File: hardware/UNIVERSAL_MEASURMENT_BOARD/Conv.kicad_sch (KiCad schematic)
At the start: 25 parts, among them U10 LMR50410YFQDBVRQ1, U7 LMR50410Y5FQDBVRQ1, U8 RAA2114034GP3#JA0, U9 LMR50410YFQDBVRQ1

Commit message: continued
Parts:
- removed D1: DS, symbol Device:D_Schottky
- removed L1, L2, L3, L4: L_Small, symbol Device:L_Small
- removed U10, U9: LMR50410YFQDBVRQ1, SOT95P280X145-6N, symbol LMR50410YFQDBVRQ1:LMR50410YFQDBVRQ1
- removed U7: LMR50410Y5FQDBVRQ1, SOT95P280X145-6N, symbol LMR50410Y5FQDBVRQ1:LMR50410Y5FQDBVRQ1
- removed U8: RAA2114034GP3#JA0, SOT95P280X110-5N, symbol RAA2114034GP3#JA0:RAA2114034GP3#JA0
- added C14, C17, C19, C20, C32, C34, C37, C38, C39, C40, C41, C42, C45, C47, C48, C50, C51, C52: 22uF, Capacitor_SMD:C_0805_2012Metric, symbol Device:C_Small
- added C15, C43: 330nF, Capacitor_SMD:C_0805_2012Metric, symbol Device:C_Small
- added C16, C35, C44, C53, C55: 100nF, Capacitor_SMD:C_0805_2012Metric, symbol Device:C_Small
- added C18, C33, C46, C49: 100nF, Capacitor_SMD:C_0603_1608Metric, symbol Device:C_Small
- added C36: 10uF, Capacitor_SMD:C_0805_2012Metric, symbol Device:C_Small
- added C54, C56: 10uF, symbol Device:C_Polarized_Small
- added C57: -F, Capacitor_SMD:C_0805_2012Metric, symbol Device:C_Small
- added F38: -A, symbol Device:Fuse_Small
- added L1, L2, L3: 68uH/1.4A, Inductor_SMD:L_TDK_VLS6045EX_VLS6045AF, symbol Samacsys_kicad_sym:SRR4028-271Y
- added R10, R12, R2, R8: 43kR, symbol Device:R
- added R11, R13, R9: -R, symbol Device:R
- added U10, U12, U7: TPS54202HDDCR, SOT95P280X110-6N, symbol TPS54202HDDCR:TPS54202HDDCR
- added U11: L7915, symbol Regulator_Linear:L7915
- added U13: ICL7662EBA+, SOIC127P600X175-8N, symbol ICL7662EBA+:ICL7662EBA+
- added U6: L7815, symbol Regulator_Linear:L7815
- added U8, U9: AMS1117-3.3, Package_TO_SOT_SMD:SOT-223-3_TabPin2, symbol Regulator_Linear:AMS1117-3.3
- C21: value 4.7uF -> 100nF; footprint (none) -> Capacitor_SMD:C_0603_1608Metric; Manufacturer_Name (none) -> --; Manufacturer_Part_Number (none) -> C0603C104J3RACTU; Mouser Part Number (none) -> --; Mouser Price/Stock (none) -> https://www.mouser.pl/ProductDetail/KEMET/C0603C104J3RACTU?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
- C22, C27, C28: footprint (none) -> Capacitor_SMD:C_0805_2012Metric; Manufacturer_Name (none) -> MCASH21GCC7684MTCA1J; Manufacturer_Part_Number (none) -> CL21A107MQYNNWE; Mouser Part Number (none) -> 810-C2012X5R1V226MAC
- C23, C26, C29: value 2.2uF -> 22uF; footprint (none) -> Capacitor_SMD:C_0805_2012Metric; Manufacturer_Name (none) -> MCASH21GCC7684MTCA1J; Manufacturer_Part_Number (none) -> CL21A107MQYNNWE; Mouser Part Number (none) -> 810-C2012X5R1V226MAC
- C24: value 100nF -> 22uF; footprint (none) -> Capacitor_SMD:C_0805_2012Metric; Manufacturer_Name (none) -> MCASH21GCC7684MTCA1J; Manufacturer_Part_Number (none) -> CL21A107MQYNNWE; Mouser Part Number (none) -> 810-C2012X5R1V226MAC
- C25, C31: value 10uF -> 22uF; footprint (none) -> Capacitor_SMD:C_0805_2012Metric; Manufacturer_Name (none) -> MCASH21GCC7684MTCA1J; Manufacturer_Part_Number (none) -> CL21A107MQYNNWE; Mouser Part Number (none) -> 810-C2012X5R1V226MAC
- C30: footprint (none) -> Capacitor_SMD:C_0603_1608Metric; Manufacturer_Name (none) -> --; Manufacturer_Part_Number (none) -> C0603C104J3RACTU; Mouser Part Number (none) -> --; Mouser Price/Stock (none) -> https://www.mouser.pl/ProductDetail/KEMET/C0603C104J3RACTU?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
- R3: value 1MR -> -R
- R4, R6: value R -> 43kR
- R5, R7: value R -> -R
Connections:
- net +12V: now also C22.1, C23.1, C24.1, C25.1, R3.2, L1.2; no longer C28.1, C31.1, R4.2, R6.2
- net +24V: now also C47.2, C48.2, C49.2, R10.1, U12.3 (VIN); no longer C21.1, C23.1, C26.1, C29.1, R3.2
- net +3.3V: now also C28.1, C29.1, U8.2 (VO); no longer C22.1
- net +5V: now also C26.1, C27.1, R7.2, C34.1, C35.1, C38.1, C39.1, C40.1, C41.1, L2.2, U8.3 (VI), U9.3 (VI); no longer C25.1
- net GND: now also C21.1, C24.2, C27.2, C31.1, R4.1, C14.2, C15.2, C16.2, C17.2, C19.1, C20.1, C32.1, C33.1, C34.2, C35.2, C36.2, C37.2, C38.2, C39.2, C40.2, C41.2, C42.2, C43.2, C44.2, C45.2, C47.1, C48.1, C49.1, C50.2, C51.2, C52.2, C53.2, C55.2, C56.1, C57.2, R12.1, R13.1, R8.1, R9.1, U10.1 (GND), U11.1 (GND), U12.1 (GND), U13.3 (GND), U6.2 (GND), U7.1 (GND), U8.1 (GND), U9.1 (GND); no longer C21.2, C31.2, R7.1
- net at C30.1: now also U10.6 (BOOT)
- net at C30.2: now also L2.1, U10.2 (SW)
- net +18V: now reaches R6.1
- net +18V: now also C21.2, C31.2, C14.1, C15.1, C19.2, C20.2, C32.2, C33.2, C52.1, C53.1, F38.2, R2.1, U10.3 (VIN), U13.8 (V+), U6.1 (IN), U7.3 (VIN); no longer R7.2
- net at R5.2: now also R3.1, U7.4 (FB); no longer R4.1
- new net: R2.2, R4.2, U7.5 (EN)
- new net: C18.1, U7.6 (BOOT)
- new net: C18.2, L1.1, U7.2 (SW)
- new net: C50.1, C51.1, F38.1, L3.2, R11.2
- new net: R10.2, R12.2, U12.5 (EN)
- new net: C54.1, U13.2 (CAP+)
- new net: C54.2, U13.4 (CAP-)
- new net: R6.2, R8.2, U10.5 (EN)
- new net: R11.1, R13.2, U12.4 (FB)
- new net: R7.1, R9.2, U10.4 (FB)
- new net: C57.1, U13.7 (OSC)
- new net: C46.1, U12.6 (BOOT)
- new net: C46.2, L3.1, U12.2 (SW)
- new net +15VA: C16.1, C17.1, U6.3 (OUT)
- new net +3.3VA: C36.1, C37.1, U9.2 (VO)
- new net -15VA: C44.1, C45.1, U11.3 (VO)
- new net -18V: C42.1, C43.1, C55.1, C56.2, U11.2 (VI), U13.5 (VOUT)
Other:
- note added: "+12V"
- note added: "+15V LDO"
- note added: "+15VA"
- note added: "+18V"
- note added: "+3.3V"
- note added: "+3.3VA"
- note added: "+5.0V"
- note added: "-15V LDO"
- note added: "-15VA"
- note added: "-18V"
- note added: "-18V INV"
- note added: "12V"
- note added: "12V DC/DC"
- note added: "18V DC/DC"
- note added: "24VIN"
- note added: "3V3 LDO"
- note added: "3V3A"
- note added: "5V"
- note added: "5V DC/DC"
- note added: "ANALOG"
- note added: "DC/DC Converters"
- note added: "DIGITAL"
- note added: "Linear Converters"
- note added: "Power Section Diagram"
- note removed: "12V0"
- note removed: "5V0"
- company: (none) -> PUT Motorsport Formula Student team
- title: (none) -> Universal Measurment Board

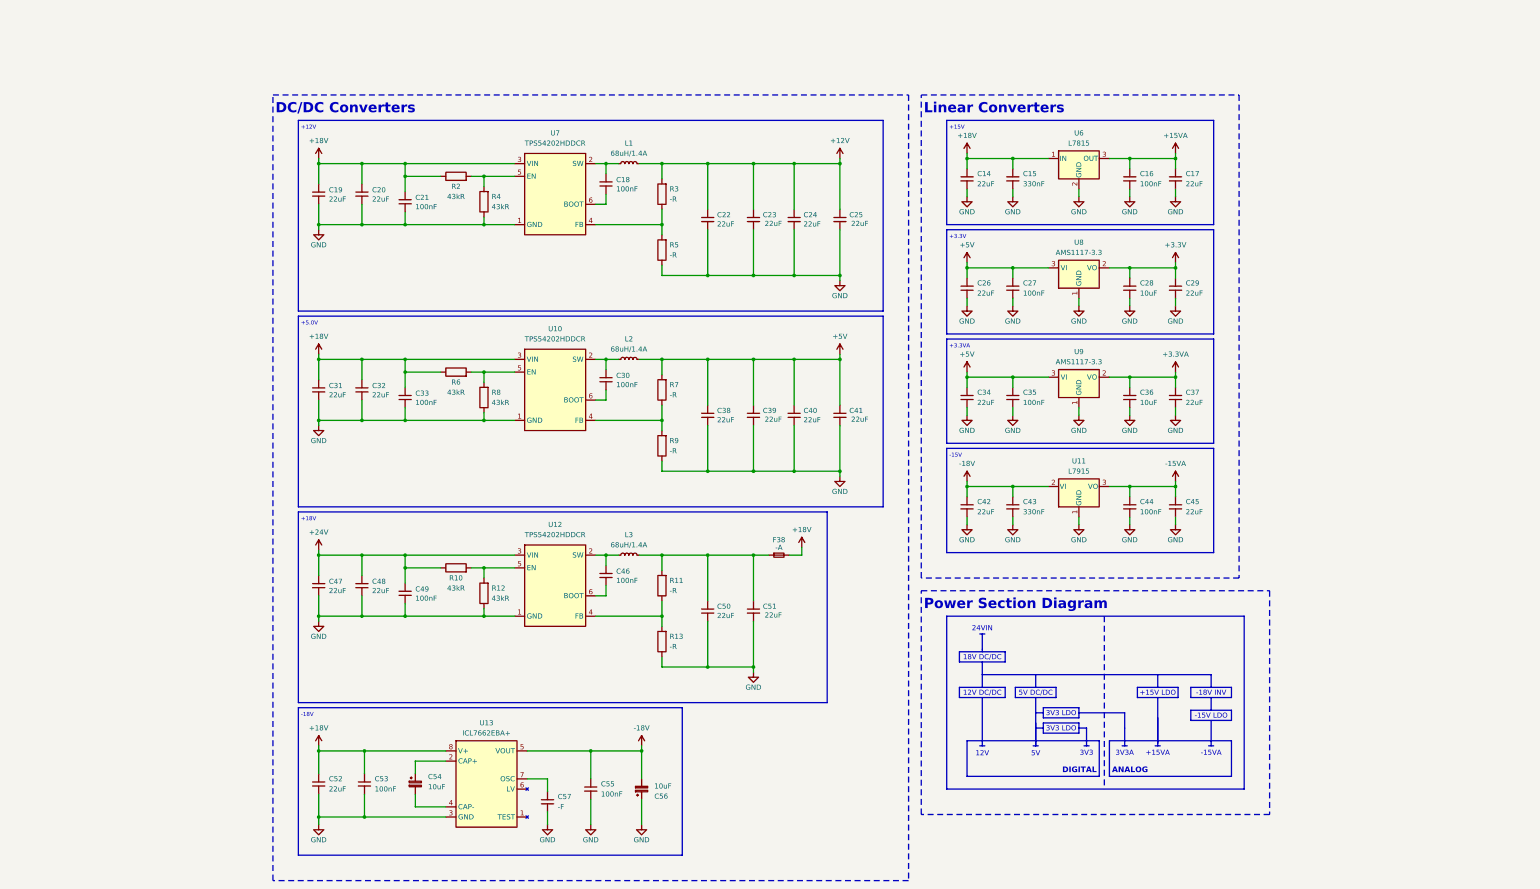
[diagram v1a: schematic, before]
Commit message: schematic review corrections
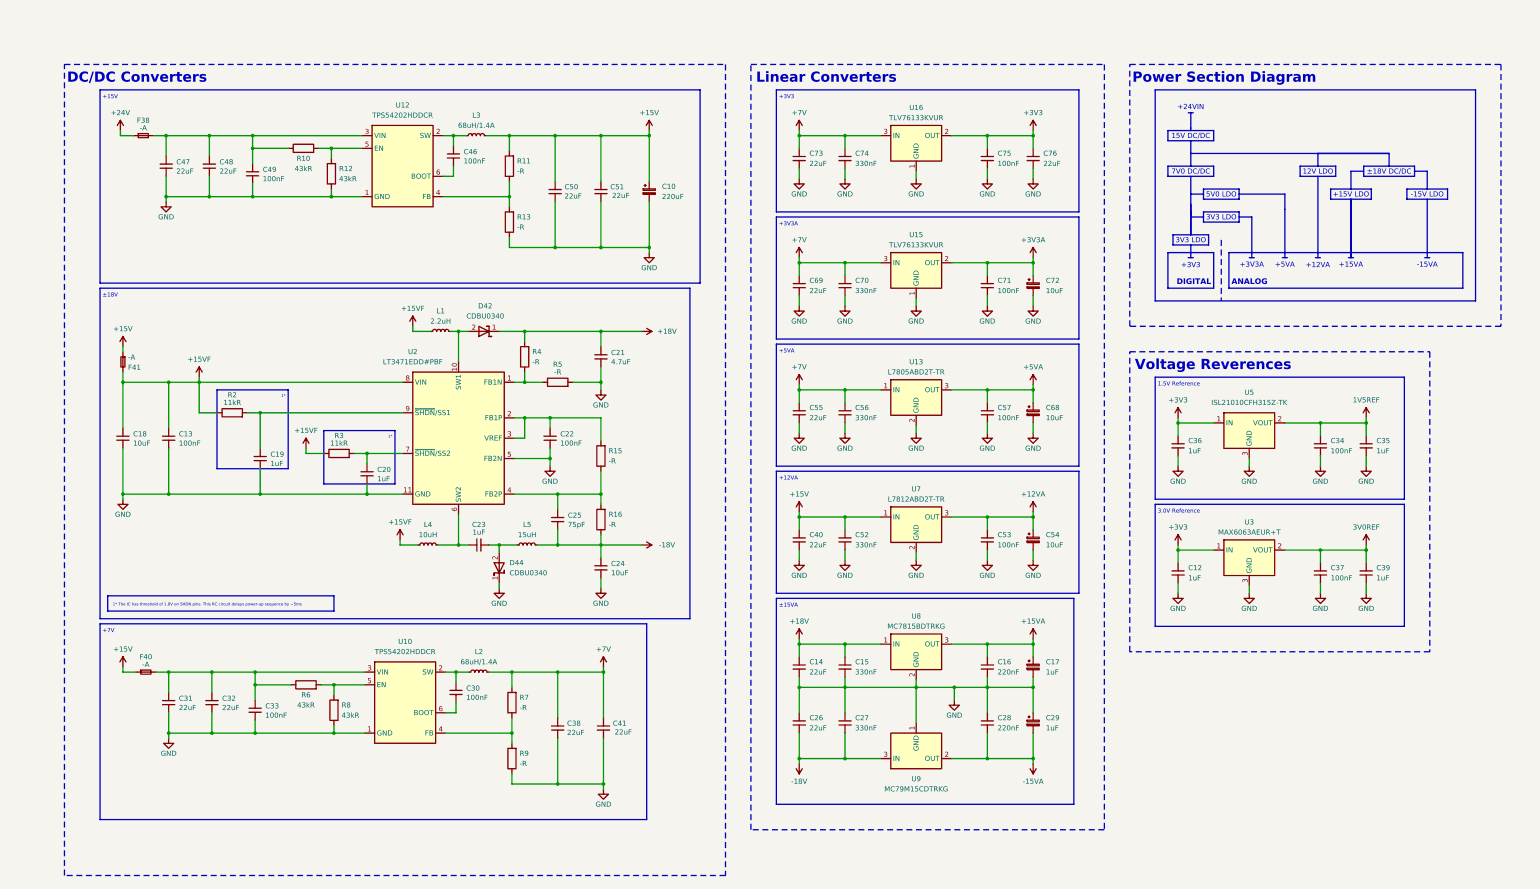
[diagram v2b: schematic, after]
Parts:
- removed C17, C29, C42, C45: 22uF, Capacitor_SMD:C_0805_2012Metric, symbol Device:C_Small
- removed C43: 330nF, Capacitor_SMD:C_0805_2012Metric, symbol Device:C_Small
- removed C44: 100nF, Capacitor_SMD:C_0805_2012Metric, symbol Device:C_Small
- removed C56: 10uF, symbol Device:C_Polarized_Small
- removed U11: L7915, symbol Regulator_Linear:L7915
- removed U13: ICL7662EBA+, SOIC127P600X175-8N, symbol ICL7662EBA+:ICL7662EBA+
- removed U6: L7815, symbol Regulator_Linear:L7815
- removed U7: TPS54202HDDCR, SOT95P280X110-6N, symbol TPS54202HDDCR:TPS54202HDDCR
- removed U8, U9: AMS1117-3.3, Package_TO_SOT_SMD:SOT-223-3_TabPin2, symbol Regulator_Linear:AMS1117-3.3
- added C10: 220uF, symbol Device:C_Polarized_Small
- added C12: 1uF, Capacitor_SMD:C_0805_2012Metric, symbol Device:C_Small
- added C13, C71, C75: 100nF, Capacitor_SMD:C_0805_2012Metric, symbol Device:C_Small
- added C17, C29: 1uF, symbol Device:C_Polarized_Small
- added C56, C70, C74: 330nF, Capacitor_SMD:C_0805_2012Metric, symbol Device:C_Small
- added C68, C72: 10uF, symbol Device:C_Polarized_Small
- added C69, C73, C76: 22uF, Capacitor_SMD:C_0805_2012Metric, symbol Device:C_Small
- added D42, D44: CDBU0340, DIOM179X85N, symbol CDBU0340:CDBU0340
- added F40, F41: -A, symbol Device:Fuse_Small
- added L4: 10uH, Inductor_SMD:L_TDK_VLS6045EX_VLS6045AF, symbol Samacsys_kicad_sym:SRR4028-271Y
- added L5: 15uH, Inductor_SMD:L_TDK_VLS6045EX_VLS6045AF, symbol Samacsys_kicad_sym:SRR4028-271Y
- added R15, R16: -R, symbol Device:R
- added U13: L7805ABD2T-TR, L7805ABD2TTR, symbol L7805ABD2T-TR:L7805ABD2T-TR
- added U15, U16: TLV76133KVUR, TLV76133KVUR, symbol TLV76133KVUR:TLV76133KVUR
- added U2: LT3471EDD#PBF, SON50P300X300X80-11N-D, symbol LT3471EDD#PBF:LT3471EDD#PBF
- added U3: MAX6063AEUR+T, SOT95P229X119-3N, symbol MAX6063AEUR+T:MAX6063AEUR+T
- added U5: ISL21010CFH315Z-TK, SOT95P237X112-3N, symbol ISL21010CFH315Z-TK:ISL21010CFH315Z-TK
- added U7: L7812ABD2T-TR, L7812ABD2TTR, symbol L7812ABD2T-TR:L7812ABD2T-TR
- added U8: MC7815BDTRKG, NVD5117PLT4GVF01, symbol MC7815BDTRKG:MC7815BDTRKG
- added U9: MC79M15CDTRKG, DPAK_(SINGLE-GAUGE)_TO-252(369C)_ISSUE_F, symbol MC79M15CDTRKG:MC79M15CDTRKG
- C16: value 100nF -> 220nF
- C18: value 100nF -> 10uF; footprint Capacitor_SMD:C_0603_1608Metric -> Capacitor_SMD:C_0805_2012Metric; Manufacturer_Name -- -> MCASH21GCC7684MTCA1J; Manufacturer_Part_Number C0603C104J3RACTU -> CL21A107MQYNNWE; Mouser Part Number -- -> 810-C2012X5R1V226MAC; Mouser Price/Stock https://www.mouser.pl/ProductDetail/KEMET/C0603C104J3RACTU?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 -> (none)
- C19, C20, C23, C39: value 22uF -> 1uF
- C21: value 100nF -> 4.7uF; footprint Capacitor_SMD:C_0603_1608Metric -> Capacitor_SMD:C_0805_2012Metric; Manufacturer_Name -- -> MCASH21GCC7684MTCA1J; Manufacturer_Part_Number C0603C104J3RACTU -> CL21A107MQYNNWE; Mouser Part Number -- -> 810-C2012X5R1V226MAC; Mouser Price/Stock https://www.mouser.pl/ProductDetail/KEMET/C0603C104J3RACTU?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 -> (none)
- C22, C34, C37: value 22uF -> 100nF
- C24: value 22uF -> 10uF
- C25: value 22uF -> 75pF
- C27: value 100nF -> 330nF
- C28: value 10uF -> 220nF
- C35: value 100nF -> 1uF
- C36: value 10uF -> 1uF
- C52: value 22uF -> 330nF
- C55: value 100nF -> 22uF
- C57: value -F -> 100nF
- L1: value 68uH/1.4A -> 2.2uH
- R2: value 43kR -> 11kR
- R3: value -R -> 11kR
- R4: value 43kR -> -R
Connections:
- net +3.3V is gone; now on net GND: C28.1
- net +15VA: now also C17.1, U8.3 (OUT)
- net +18V: now also R4.2, D42.1 (K), U8.1 (IN); no longer C19.2, C20.2, C31.2, C32.2, C33.2, C52.1, C53.1, F38.2, R2.1, R6.1, U10.3 (VIN)
- net +24V: now also F38.1; no longer C47.2, C48.2, C49.2, R10.1, U12.3 (VIN)
- net -15VA: now also C28.2, C29.2, U9.2 (OUT)
- net -18V: now also C24.2, C25.1, C26.2, C27.2, L5.2, R16.1, U9.3 (IN); no longer C55.1
- net GND: now also C18.1, C22.1, C24.1, C26.1, C27.1, C54.2, R5.2, C10.2, C12.2, C13.1, C17.2, C29.1, C56.2, C68.2, C69.2, C70.2, C71.2, C72.2, C73.2, C74.2, C75.2, C76.2, D44.1 (K), U13.2 (GND), U15.1 (GND), U16.1 (GND), U2.11 (GND), U2.5 (FB2N), U3.3 (GND), U5.3 (GND), U7.2 (GND), U8.2 (GND), U9.1 (GND); no longer C22.2, C23.2, C24.2, C25.2, C26.2, C27.2, C28.2, R4.1, R5.1
- net at R2.2: now also C19.2, U2.9 (~{SHDN}/SS1); no longer R4.2
- net +15VF: now reaches C18.2, L1.1
- net +15VF: now also R2.1, R3.1, C13.2, F41.2, L4.1, U2.8 (VIN)
- net +15V: now reaches C50.1, C51.1, L3.2, R11.2
- net +15V: now also C40.1, C52.1, C10.1, F40.1, F41.1, U7.1 (IN); no longer F38.1
- net +12VA: now reaches C54.1
- net +12VA: now also C53.1, U7.3 (OUT)
- net +5VA: now reaches C57.1
- net +5VA: now also C68.1, U13.3 (OUT)
- removed net +12V: C22.1, C23.1, C24.1, C25.1, L1.2, R3.2
- net +3.3VA renamed +3V3
- net +3V3: now also C12.1, C75.1, C76.1, U16.2 (OUT), U3.1 (IN), U5.1 (IN); no longer C37.1
- removed net +5V: C26.1, C27.1, C34.1, C35.1, C38.1, C39.1, C40.1, C41.1, L2.2, R7.2
- new net: C20.2, R3.2, U2.7 (~{SHDN}/SS2)
- new net: D42.2 (A), L1.2, U2.10 (SW1)
- new net: C47.2, C48.2, C49.2, F38.2, R10.1, U12.3 (VIN)
- new net: C31.2, C32.2, C33.2, F40.2, R6.1, U10.3 (VIN)
- new net: R4.1, R5.1, U2.1 (FB1N)
- new net: C22.2, R15.2, U2.2 (FB1P), U2.3 (VREF)
- new net: C25.2, R15.1, R16.2, U2.4 (FB2P)
- new net: C23.2, L4.2, U2.6 (SW2)
- new net: C23.1, D44.2 (A), L5.1
- new net +3V3A: C71.1, C72.1, U15.2 (OUT)
- new net +7V: C38.1, C41.1, C55.1, C56.1, C69.1, C70.1, C73.1, C74.1, L2.2, R7.2, U13.1 (IN), U15.3 (IN), U16.3 (IN)
- new net 1V5REF: C34.1, C35.1, U5.2 (VOUT)
- new net 3V0REF: C37.1, C39.1, U3.2 (VOUT)
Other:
- note added: "+12VA"
- note added: "+24VIN"
- note added: "+3V3"
- note added: "+3V3A"
- note added: "+5VA"
- note added: "+7V"
- note added: "1*"
- note added: "1* The IC has threshold of 1.8V on SHDN pins. This RC circuit delays power-up sequence by ~5ms"
- note added: "1.5V Reference"
- note added: "12V LDO"
- note added: "15V DC/DC"
- note added: "3.0V Reference"
- note added: "5V0 LDO"
- note added: "7V0 DC/DC"
- note added: "Voltage Reverences"
- note added: "±15VA"
- note added: "±18V"
- note added: "±18V DC/DC"
- note removed: "+12V"
- note removed: "+18V"
- note removed: "+3.3V"
- note removed: "+3.3VA"
- note removed: "+5.0V"
- note removed: "-15V"
- note removed: "-18V"
- note removed: "-18V INV"
- note removed: "12V"
- note removed: "12V DC/DC"
- note removed: "18V DC/DC"
- note removed: "24VIN"
- note removed: "3V3"
- note removed: "3V3A"
- note removed: "5V"
- note removed: "5V DC/DC"
- moved on the sheet: C46, C47, C48, C49, C50, C51, F38, L3, R10, R11, R12, R13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

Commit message: final schematic review corrections
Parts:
- added TP10: 12VA, symbol Connector:TestPoint
- added TP11: 5VA, symbol Connector:TestPoint
- added TP12: 3V3A, symbol Connector:TestPoint
- added TP13: 3V3, symbol Connector:TestPoint
- added TP14: 3V0A, symbol Connector:TestPoint
- added TP15: 1V5A, symbol Connector:TestPoint
- added TP4: M15V, symbol Connector:TestPoint
- added TP5: 18V, symbol Connector:TestPoint
- added TP6: -18V, symbol Connector:TestPoint
- added TP7: 7V, symbol Connector:TestPoint
- added TP8: 15VA, symbol Connector:TestPoint
- added TP9: -15VA, symbol Connector:TestPoint
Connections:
- net +3V3: now also TP13.1; no longer C12.1, C36.1, U3.1 (IN), U5.1 (IN)
- net +3V3A: now also C36.1, U5.1 (IN), TP12.1
- net +12VA renamed +12V0A
- net +12V0A: now also TP10.1
- net +15V renamed +15V0
- net +15V0: now also TP4.1
- net +15VA renamed +15V0A
- net +15V0A: now also TP8.1
- net +15VF renamed +15V0F
- net +18V renamed +18V0
- net +18V0: now also TP5.1
- net +24V renamed +24V0
- net +5VA renamed +5V0A
- net +5V0A: now also C12.1, U3.1 (IN), TP11.1
- net +7V renamed +7V0
- net +7V0: now also TP7.1
- net -15VA renamed -15V0A
- net -15V0A: now also TP9.1
- net -18V renamed -18V0
- net -18V0: now also TP6.1
- net 1V5REF renamed +1V5A
- net +1V5A: now also TP15.1
- net 3V0REF renamed +3V0A
- net +3V0A: now also TP14.1
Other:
- note added: "+12V0A"
- note added: "+15V0A"
- note added: "+1V5A"
- note added: "+3V0A"
- note added: "+5V0A"
- note added: "-15V0A"
- note added: "1V5 REF"
- note added: "3V0 REF"
- note removed: "+15VA"
- note removed: "-15VA"
- moved on the sheet: C10, C12, C13, C14, C15, C16, C17, C18, C19, C20, C21, C22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
